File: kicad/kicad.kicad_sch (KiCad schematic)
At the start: 20 parts, among them J101 NOTIFY_LED_CONN, J102 EPD_SPI_CONN, J103 HPC_CONN, J104 USBC_CONN, J105 MGMT_CONN, J106 GLOBAL_CONN, J107 INPUT_CONN

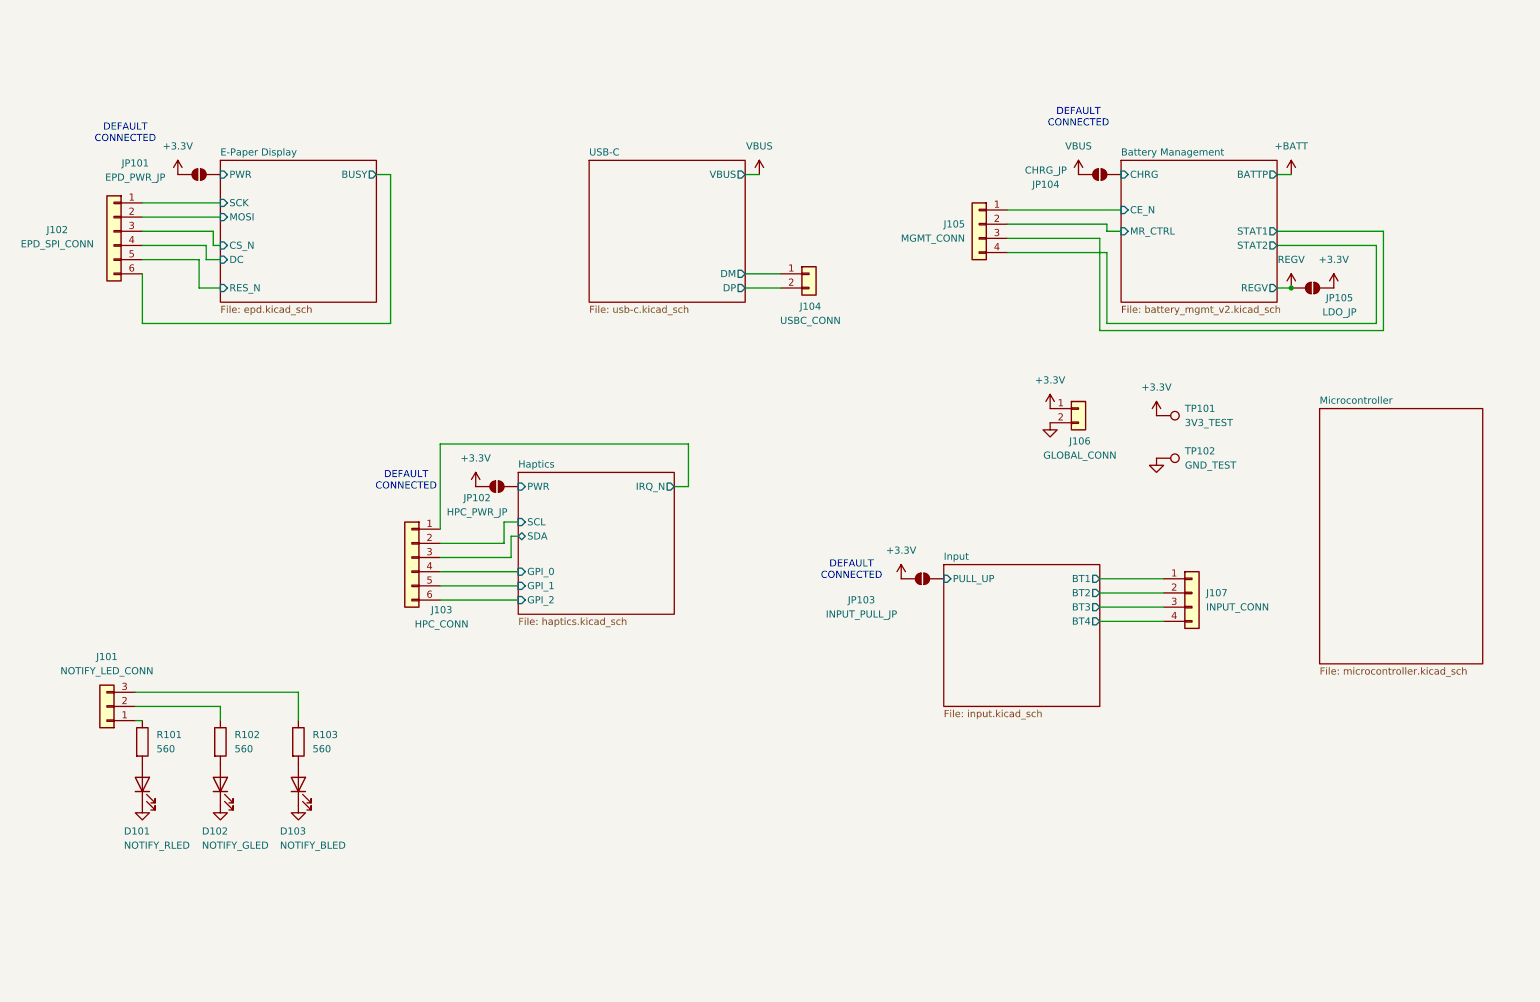
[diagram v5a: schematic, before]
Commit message: Start removing debug and integrate microcontroller
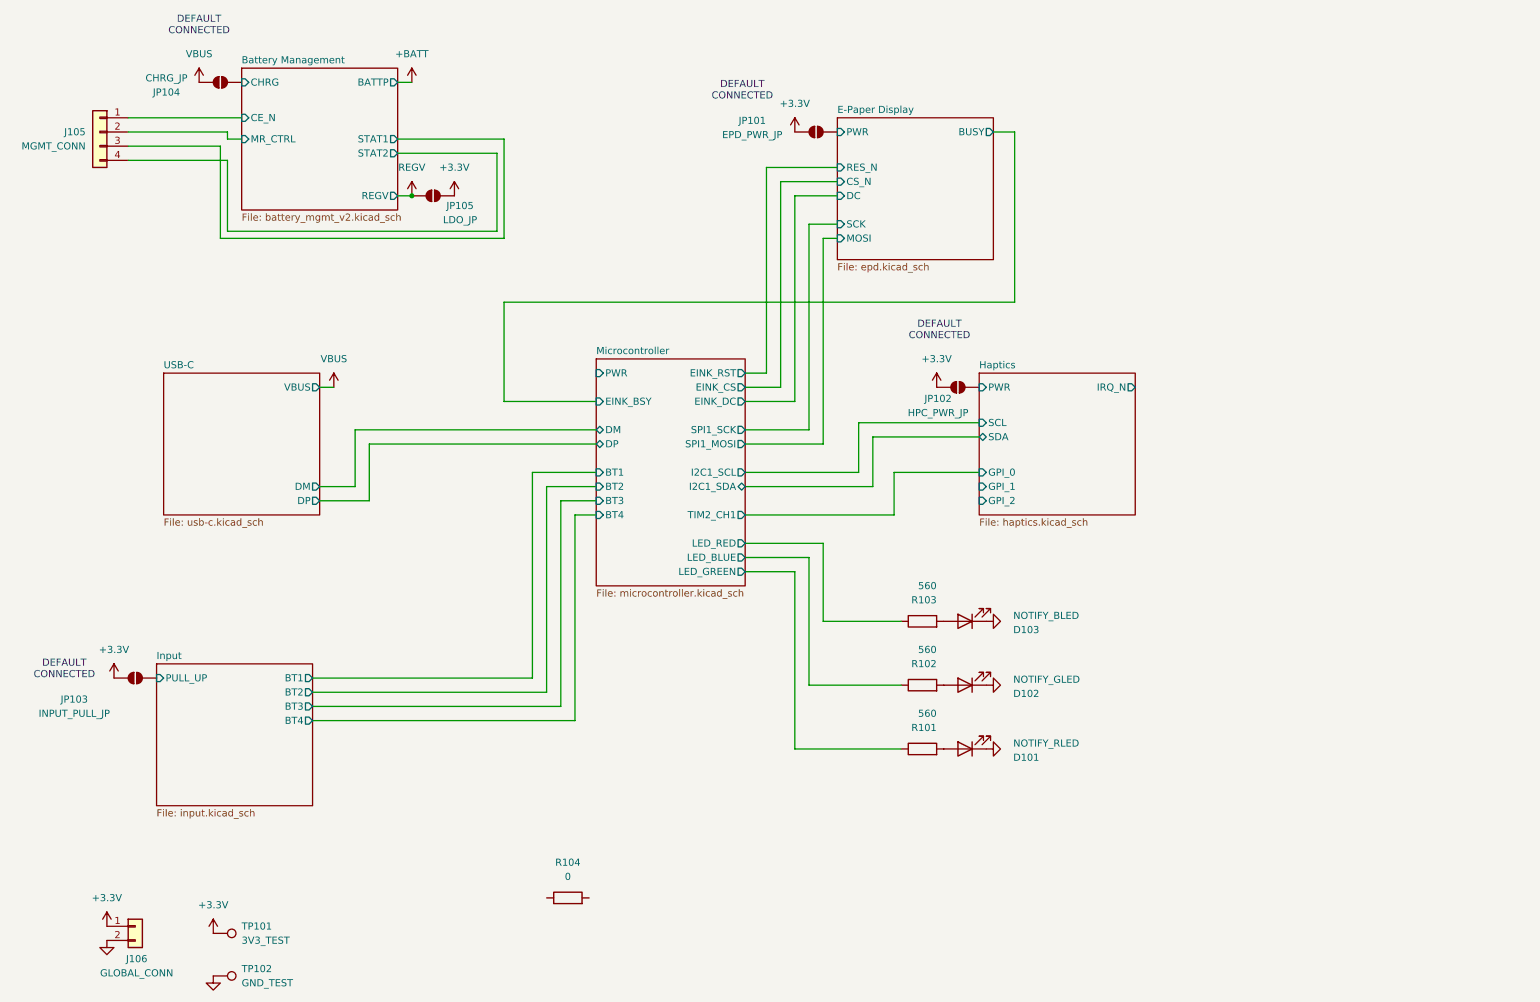
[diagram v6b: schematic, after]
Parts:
- removed J101: NOTIFY_LED_CONN, Connector_JST:JST_XH_B3B-XH-A_1x03_P2.50mm_Vertical, symbol Connector_Generic:Conn_01x03
- removed J102: EPD_SPI_CONN, Connector_JST:JST_XH_B6B-XH-A_1x06_P2.50mm_Vertical, symbol Connector_Generic:Conn_01x06
- removed J103: HPC_CONN, Connector_JST:JST_XH_B6B-XH-A_1x06_P2.50mm_Vertical, symbol Connector_Generic:Conn_01x06
- removed J104: USBC_CONN, Connector_JST:JST_XH_B2B-XH-A_1x02_P2.50mm_Vertical, symbol Connector_Generic:Conn_01x02
- removed J107: INPUT_CONN, Connector_JST:JST_XH_B4B-XH-A_1x04_P2.50mm_Vertical, symbol Connector_Generic:Conn_01x04
- added R104: 0, symbol Device:R
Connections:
- net Microcontroller/LED_RED: now reaches R103.1
- net Microcontroller/LED_GREEN: now reaches R101.1
- net Microcontroller/LED_BLUE: now reaches R102.1
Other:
- sheet Microcontroller ports: added BT1, BT2, BT3, BT4, DM, DP, EINK_BSY, EINK_CS, EINK_DC, EINK_RST, I2C1_SCL, I2C1_SDA, LED_BLUE, LED_GREEN, LED_RED, PWR, SPI1_MOSI, SPI1_SCK, TIM2_CH1; removed none
- moved on the sheet: D101, D102, D103, J105, J106, JP101, JP102, JP103, JP104, JP105, R101, R102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

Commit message: Microcontroller additions
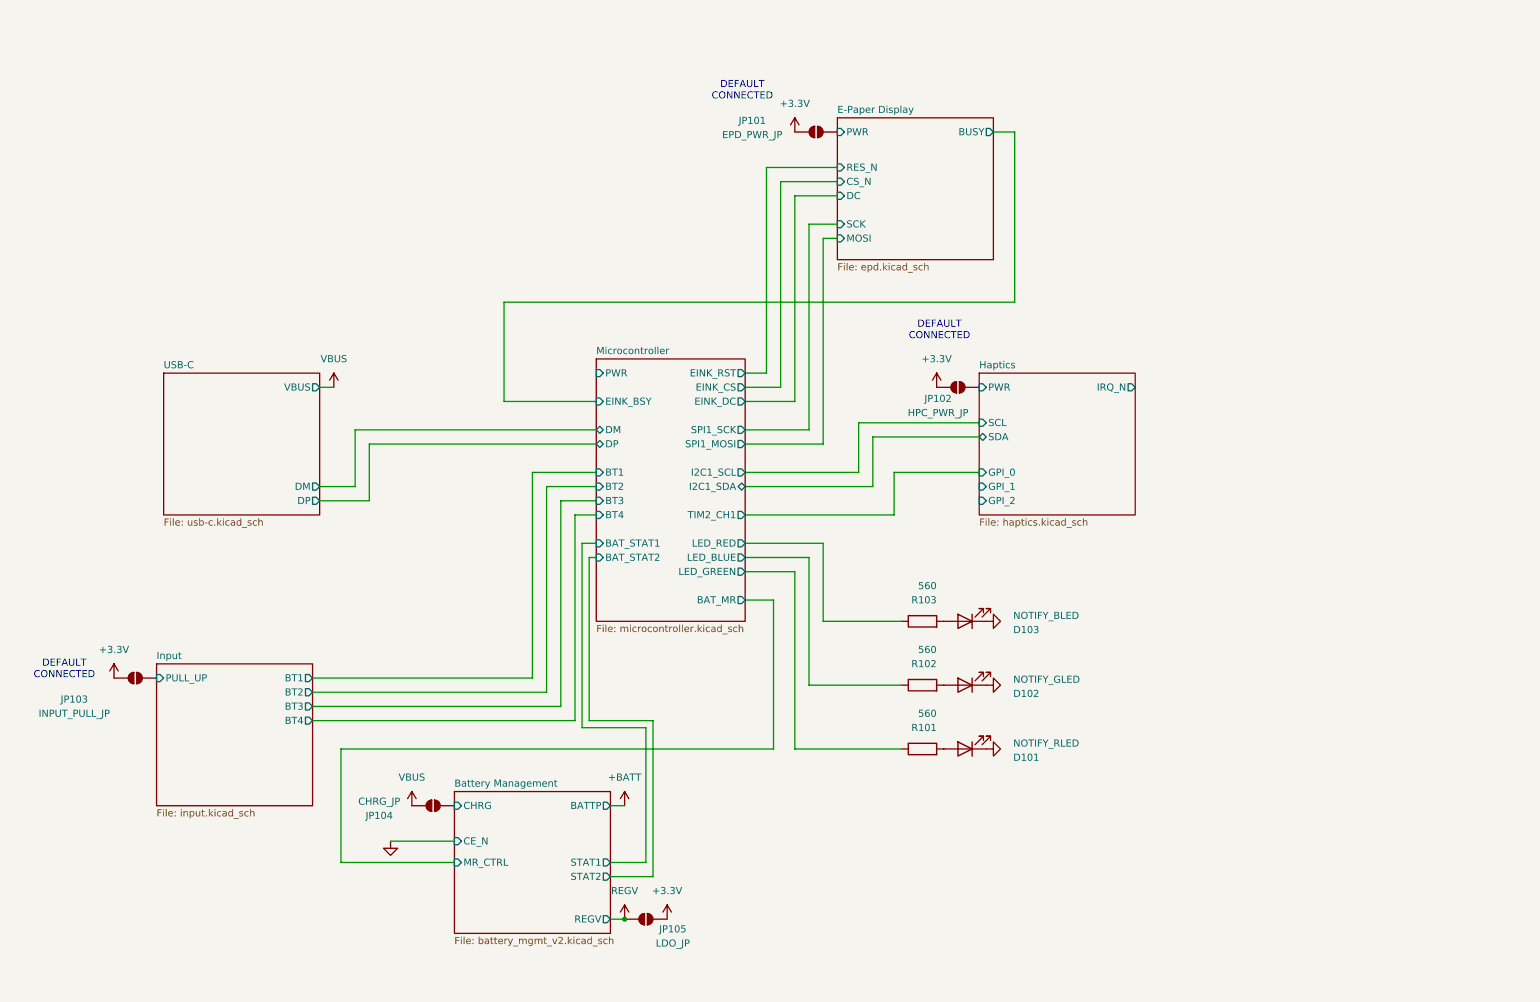
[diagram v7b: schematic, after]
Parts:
- removed J105: MGMT_CONN, Connector_JST:JST_XH_B4B-XH-A_1x04_P2.50mm_Vertical, symbol Connector_Generic:Conn_01x04
- removed J106: GLOBAL_CONN, Connector_JST:JST_XH_B2B-XH-A_1x02_P2.50mm_Vertical, symbol Connector_Generic:Conn_01x02
- removed R104: 0, symbol Device:R
- removed TP101: 3V3_TEST, TestPoint:TestPoint_Pad_D1.5mm, symbol Connector:TestPoint
- removed TP102: GND_TEST, TestPoint:TestPoint_Pad_D1.5mm, symbol Connector:TestPoint
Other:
- sheet Microcontroller ports: added BAT_MR, BAT_STAT1, BAT_STAT2; removed none
- moved on the sheet: JP104, JP105

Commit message: Unfinished switch additions and fixes
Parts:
- removed JP101: EPD_PWR_JP, Jumper:SolderJumper-2_P1.3mm_Open_TrianglePad1.0x1.5mm, symbol Jumper:SolderJumper_2_Open
- removed JP102: HPC_PWR_JP, Jumper:SolderJumper-2_P1.3mm_Open_TrianglePad1.0x1.5mm, symbol Jumper:SolderJumper_2_Open
- removed JP103: INPUT_PULL_JP, Jumper:SolderJumper-2_P1.3mm_Open_TrianglePad1.0x1.5mm, symbol Jumper:SolderJumper_2_Open
- removed JP104: CHRG_JP, Jumper:SolderJumper-2_P1.3mm_Open_TrianglePad1.0x1.5mm, symbol Jumper:SolderJumper_2_Open
- removed JP105: LDO_JP, Jumper:SolderJumper-2_P1.3mm_Open_TrianglePad1.0x1.5mm, symbol Jumper:SolderJumper_2_Open
- added R104: 0, Raven:JS102000SAQN, symbol Device:R
- added R105, R106, R108, R109: 0, symbol Device:R
- added SW102: PWR_SWITCH, Raven:JS102000SAQN, symbol Switch:SW_SPDT
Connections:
- net +3.3V: now also R105.1, R106.2, R108.1, R109.2, SW102.2 (B)
- net Battery Management/CHRG: now also R104.2
- net E-Paper Display/PWR: now also R109.1
- net GND: now also SW102.3 (C)
- net Haptics/PWR: now also R105.2
- net Input/PULL_UP: now also R106.1
- net Microcontroller/PWR: now also R108.2
- net REGV: now also SW102.1 (A)
- net VBUS: now also R104.1
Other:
- note removed: "DEFAULT CONNECTED"
